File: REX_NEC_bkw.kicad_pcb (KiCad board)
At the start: 2 copper layers, 16.4 x 34.2 mm, 9 parts, among them J1 DIP28 legs 27C256, J2 JTAG, J3 PRG, U1 XCR3064-VQ44, U2 29F800, U3 LP2980

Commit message: names
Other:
- board text added: "NEC"
- board text removed: "8201"
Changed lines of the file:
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@@
     (34 B.Paste user hide)
     (35 F.Paste user hide)
-    (36 B.SilkS user hide)
-    (37 F.SilkS user hide)
+    (36 B.SilkS user)
+    (37 F.SilkS user)
     (38 B.Mask user hide)
     (39 F.Mask user hide)
@@
     (add_net /e~OE)
     (add_net GND)
-    (add_net "Net-(J1-Pad1)")
-    (add_net "Net-(U1-Pad11)")
-    (add_net "Net-(U1-Pad3)")
-    (add_net "Net-(U1-Pad35)")
-    (add_net "Net-(U1-Pad42)")
-    (add_net "Net-(U1-Pad43)")
-    (add_net "Net-(U1-Pad44)")
-    (add_net "Net-(U3-Pad4)")
   )
   (module 000_LOCAL:R_0805 (layer Top)
@@
     (effects (font (size 0.8 0.8) (thickness 0.1)) (justify left bottom))
   )
-  (gr_text 8201 (at 149.3266 108.6866 -90) (layer F.SilkS)
+  (gr_text NEC (at 149.1234 108.5215 -90) (layer F.SilkS)
     (effects (font (size 1.2 1.2) (thickness 0.2)) (justify bottom))
   )
@@
     (effects (font (size 1.016 1.016) (thickness 0.1016)) (justify left bottom))
   )
-  (via (at 151.8158 98.3742) (size 0.4064) (drill 0.254) (layers Top Bottom) (net 28))
   (segment (start 143.408 83.5406) (end 143.408 88.06) (width 0.4064) (layer Bottom) (net 1))
   (segment (start 151.968 89.437) (end 151.968 89.0285) (width 0.1778) (layer Bottom) (net 1))
@@
   (segment (start 154.1145 99.06) (end 153.7335 98.679) (width 0.1778) (layer Top) (net 27))
   (segment (start 153.7335 98.679) (end 153.7335 86.3215) (width 0.1778) (layer Top) (net 27))
+  (via (at 151.8158 98.3742) (size 0.4064) (drill 0.254) (layers Top Bottom) (net 28))
   (segment (start 145.948 83.8454) (end 145.968 83.8654) (width 0.1778) (layer Top) (net 28))
   (segment (start 145.968 83.8654) (end 145.968 85.537) (width 0.4064) (layer Top) (net 28))

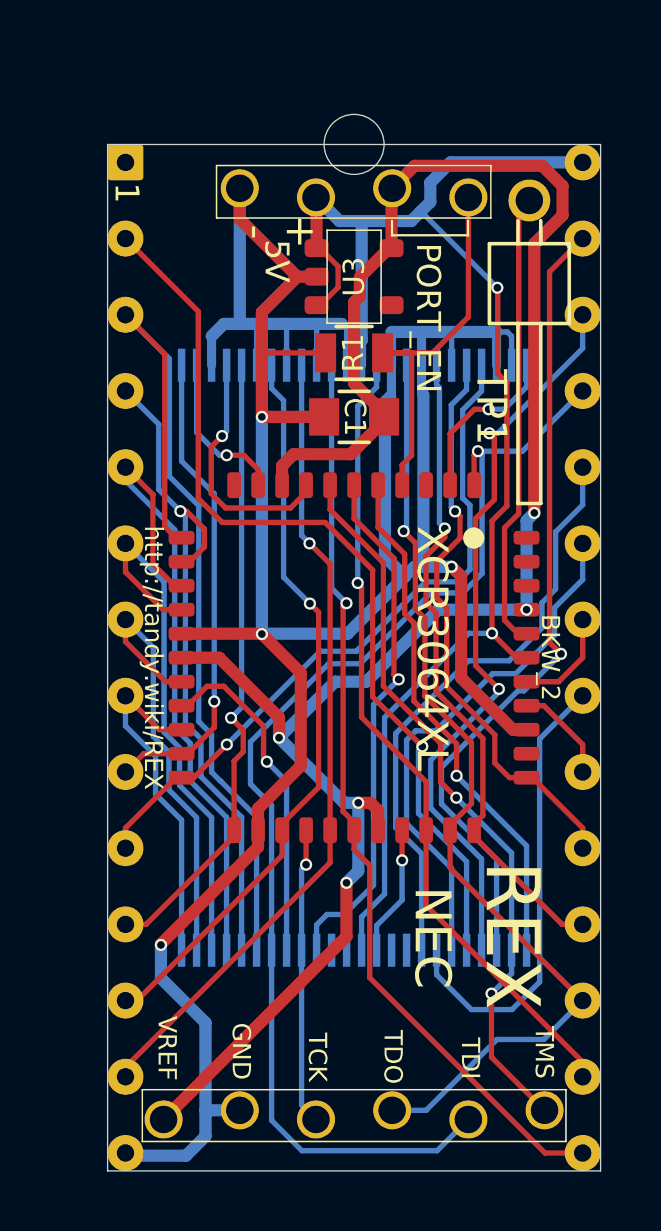
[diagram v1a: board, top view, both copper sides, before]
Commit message: remove some sharp inside angles. move c1 on nec.
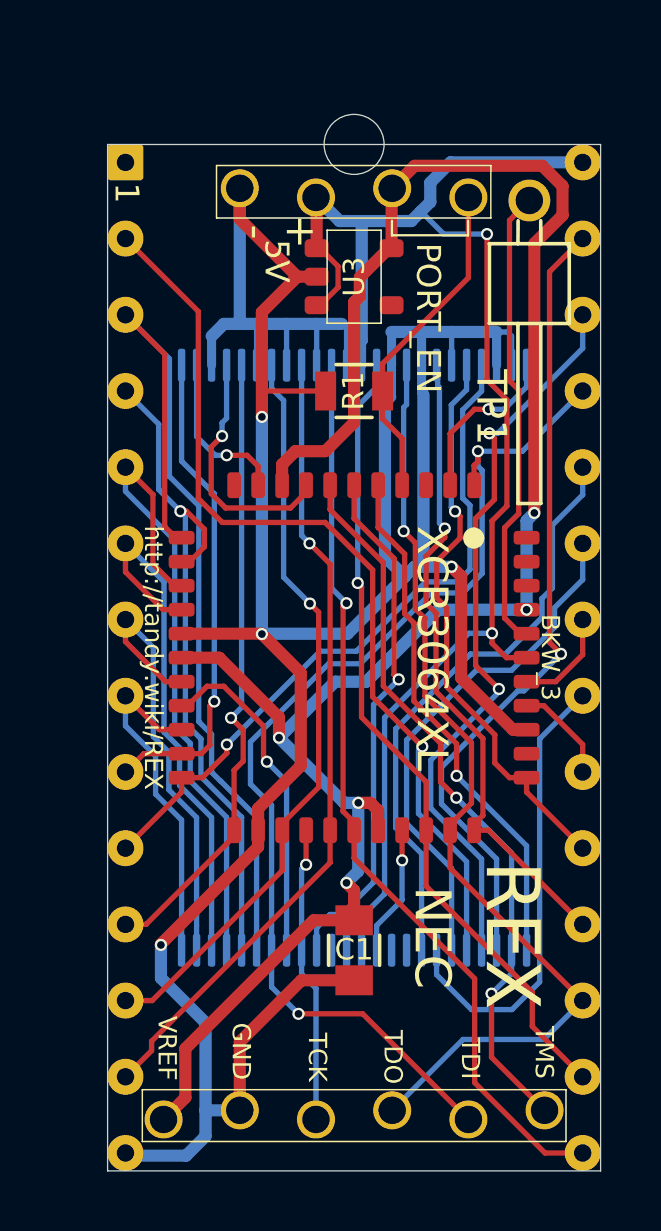
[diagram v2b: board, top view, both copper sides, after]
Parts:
- moved C1 17.8 mm to (147.2, 108.9), turned to 270 degrees
- moved R1 1.27 mm to (147.2, 90.3)
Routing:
- net GND: track 101.2 -> 106.9 mm
- net /eA8: track 40.0 -> 36.5 mm, vias 1 -> 2
- net /PORT_EN: track 12.8 -> 11.0 mm
- net +5V: track 49.3 -> 50.3 mm
- net +3V3: track 67.4 -> 66.9 mm
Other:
- board text added: "BKW_3"
- board text added: "R1: 10K"
- board text removed: "BKW_2"
- board text removed: "R1: 47K"

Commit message: v13
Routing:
- net +3V3: track 66.9 -> 62.7 mm, vias 5 -> 7
- net /TMS: track 24.4 -> 23.8 mm
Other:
- board size 16.4 x 34.2 mm -> 16.3 x 34 mm
- board text added: "BKW_4"
- board text removed: "BKW_3"

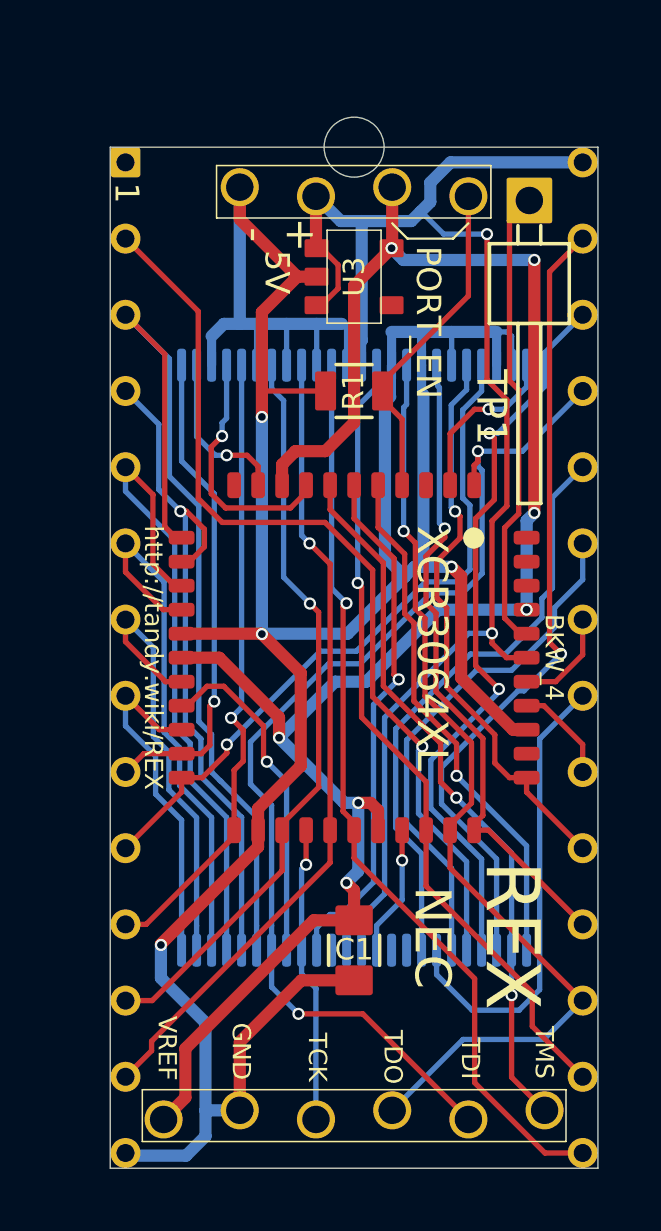
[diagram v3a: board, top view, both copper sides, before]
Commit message: flip ram and reroute nec board, several other minor touches both boards
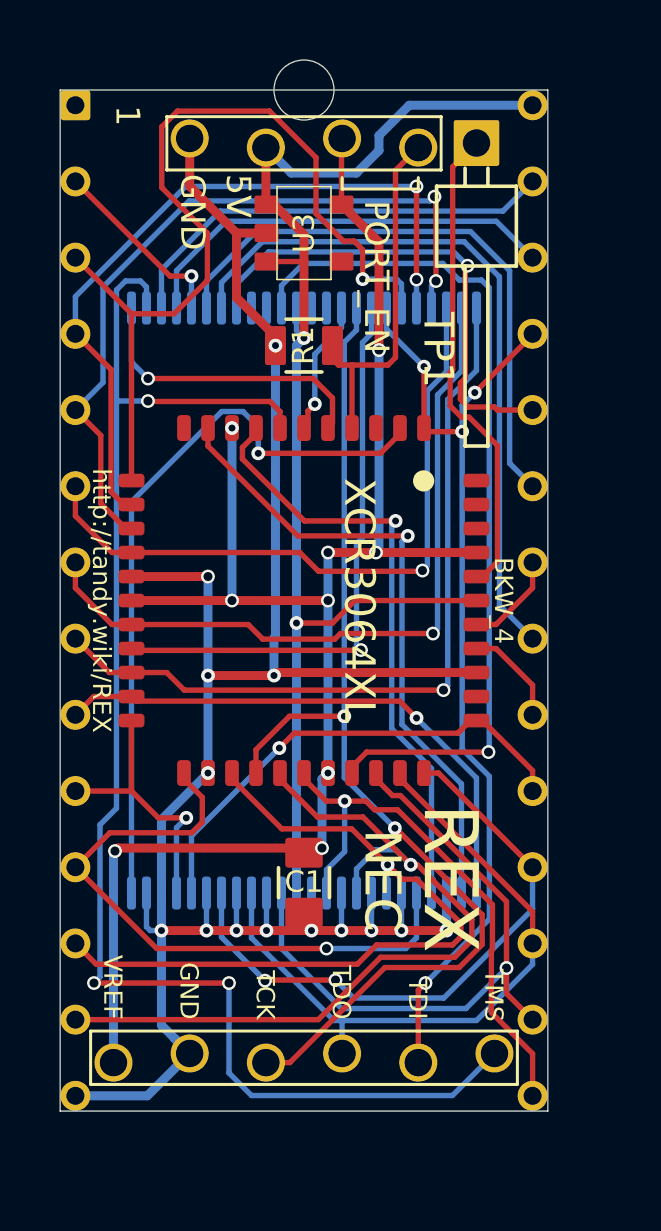
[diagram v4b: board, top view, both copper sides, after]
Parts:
- R1: value 10k -> 47k
- moved C1 2.81 mm to (145.5, 106.7)
- moved TP1 2.60 mm to (151.3, 82.0)
- moved J1 2.53 mm to (145.5, 97.3)
- moved U1 2.53 mm to (145.5, 97.3)
- moved U2 2.53 mm to (145.5, 97.3), turned to 270 degrees
- moved J2 2.53 mm to (145.5, 112.5)
- moved J3 2.33 mm to (145.5, 82.0)
- moved R1 2.25 mm to (145.5, 88.8)
- moved U3 2.21 mm to (145.5, 85.0)
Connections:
- U3 pad 3: +5V -> (no net)
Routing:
- net GND: track 106.9 -> 76.2 mm, vias 4 -> 14
- net /TCK: track 9.90 -> 36.3 mm, vias 1 -> 2
- net /TMS: track 23.8 -> 48.7 mm, vias 2 -> 3
- net /_~WE: track 4.35 -> 28.8 mm
- net /eA12: track 30.5 -> 6.24 mm
- net /_A16: track 5.64 -> 24.8 mm
- net /_~CE: track 5.47 -> 21.3 mm
- net /eA2: track 11.6 -> 26.2 mm, vias 0 -> 1
- net /eA0: track 22.9 -> 9.06 mm
- net /_RY~BY: track 17.5 -> 4.52 mm
- net /eD3: track 30.6 -> 18.5 mm
- net /eA14: track 26.9 -> 14.9 mm, vias 1 -> 0
- net /_~OE: track 8.31 -> 20.2 mm
- net /eA13: track 24.9 -> 14.3 mm, vias 2 -> 0
- net /eD5: track 32.1 -> 22.1 mm, vias 1 -> 0
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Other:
- net class Default: clearance 0.1778 -> 0.16; trace_width 0.1778 -> 0.18; via_dia 0.4064 -> 0.46; via_drill 0.254 -> 0.3
- net class Power added: clearance 0.16, trace_width 0.3, via_dia 0.46, via_drill 0.3
- rule trace_clearance: 0.1778 -> 0.16
- rule trace_min: 0.1778 -> 0.18
- rule via_min_drill: 0.254 -> 0.3
- rule via_min_size: 0.381 -> 0.46
- board text added: "DQ10"
- board text added: "DQ11"
- board text added: "DQ12"
- board text added: "DQ13"
- board text added: "DQ14"
- board text added: "DQ8"
- board text added: "DQ9"
- board text added: "R1: 47K"
- board text added: "~BYTE"
- board text added: "~RESET"
- board text removed: "+"
- board text removed: "-"
- board text removed: "R1: 10K"
